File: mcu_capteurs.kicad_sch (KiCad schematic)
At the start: 71 parts, among them J15 BOOT0, J4 STLINK, SW1 435431019840, U2 TCA9517DR, U3 WSEN-PDUS, U4 STM32G474CEUx, Y1 16 MHz

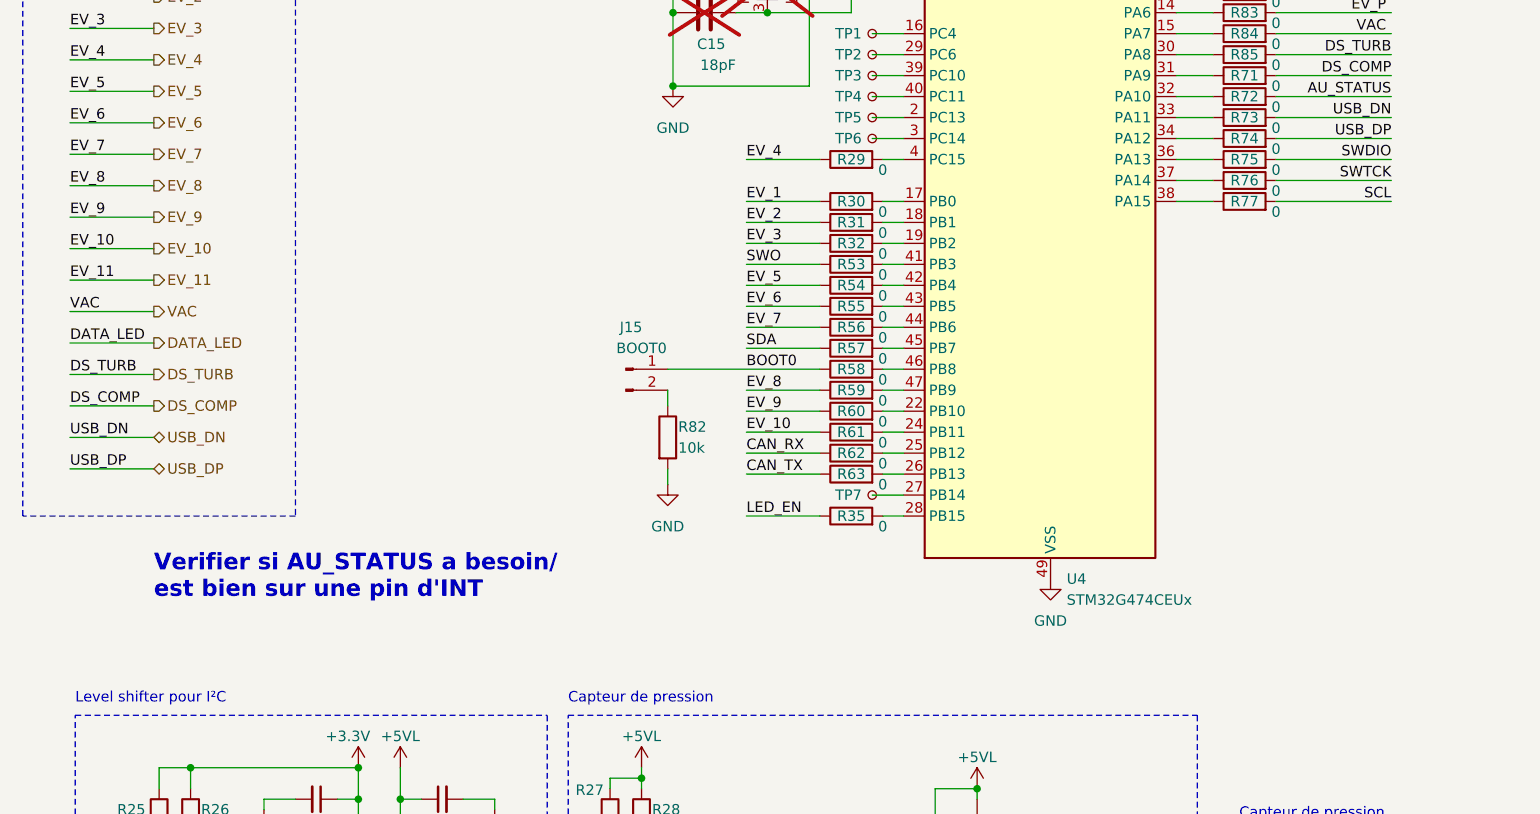
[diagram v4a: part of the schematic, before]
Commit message: placement en cours, remplacement diode schotcky, customisation empreinte capteur pression, suppression R pour les signaux figé du uC (SW, BOOT, etc). TODO avancer placement, ajouter LED
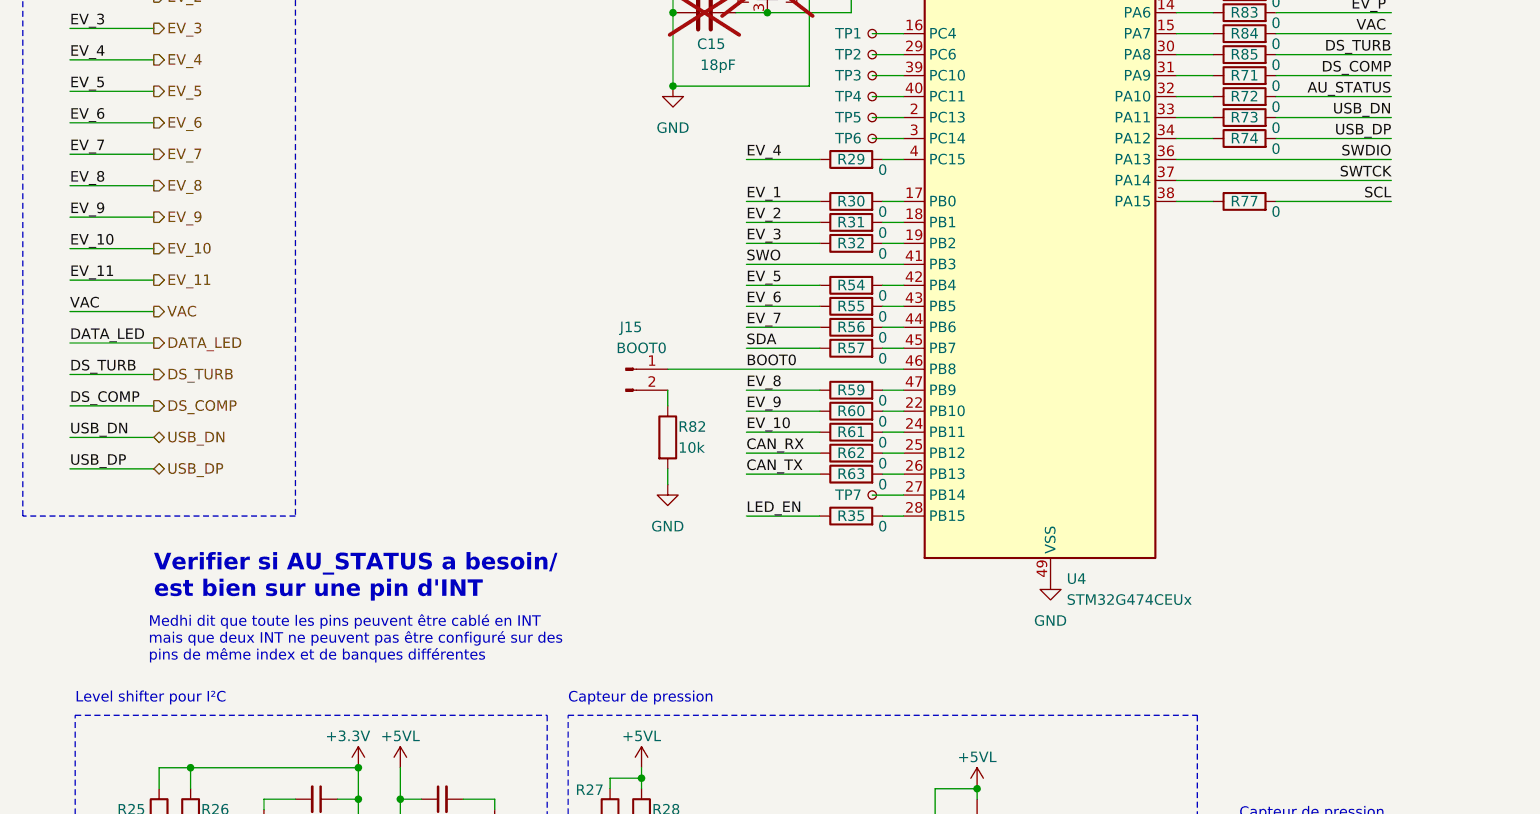
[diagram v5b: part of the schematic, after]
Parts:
- removed R53, R58, R75, R76: 0, Resistor_SMD:R_0402_1005Metric, symbol Device:R
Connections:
- net BOOT0: now also U4.46 (PB8)
- net SWDIO: now also U4.36 (PA13)
- net SWO: now also U4.41 (PB3)
- net SWTCK: now also U4.37 (PA14)
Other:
- note added: "Medhi dit que toute les pins peuvent être cablé en INT mais que deux INT ne peuvent pas être configuré sur des pins de même index et de banques différentes"

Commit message: placement composant (carte distributeur)
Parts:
- U4: footprint Package_DFN_QFN:QFN-48-1EP_7x7mm_P0.5mm_EP5.6x5.6mm -> 12V-actuators_pcb:QFN-48-1EP_7x7mm_P0.5mm_EP5.5x5.5mm
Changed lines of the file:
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@@
 			)
 		)
-		(property "Footprint" "Package_DFN_QFN:QFN-48-1EP_7x7mm_P0.5mm_EP5.6x5.6mm"
+		(property "Footprint" "12V-actuators_pcb:QFN-48-1EP_7x7mm_P0.5mm_EP5.5x5.5mm"
 			(at 127 129.54 0)
 			(effects

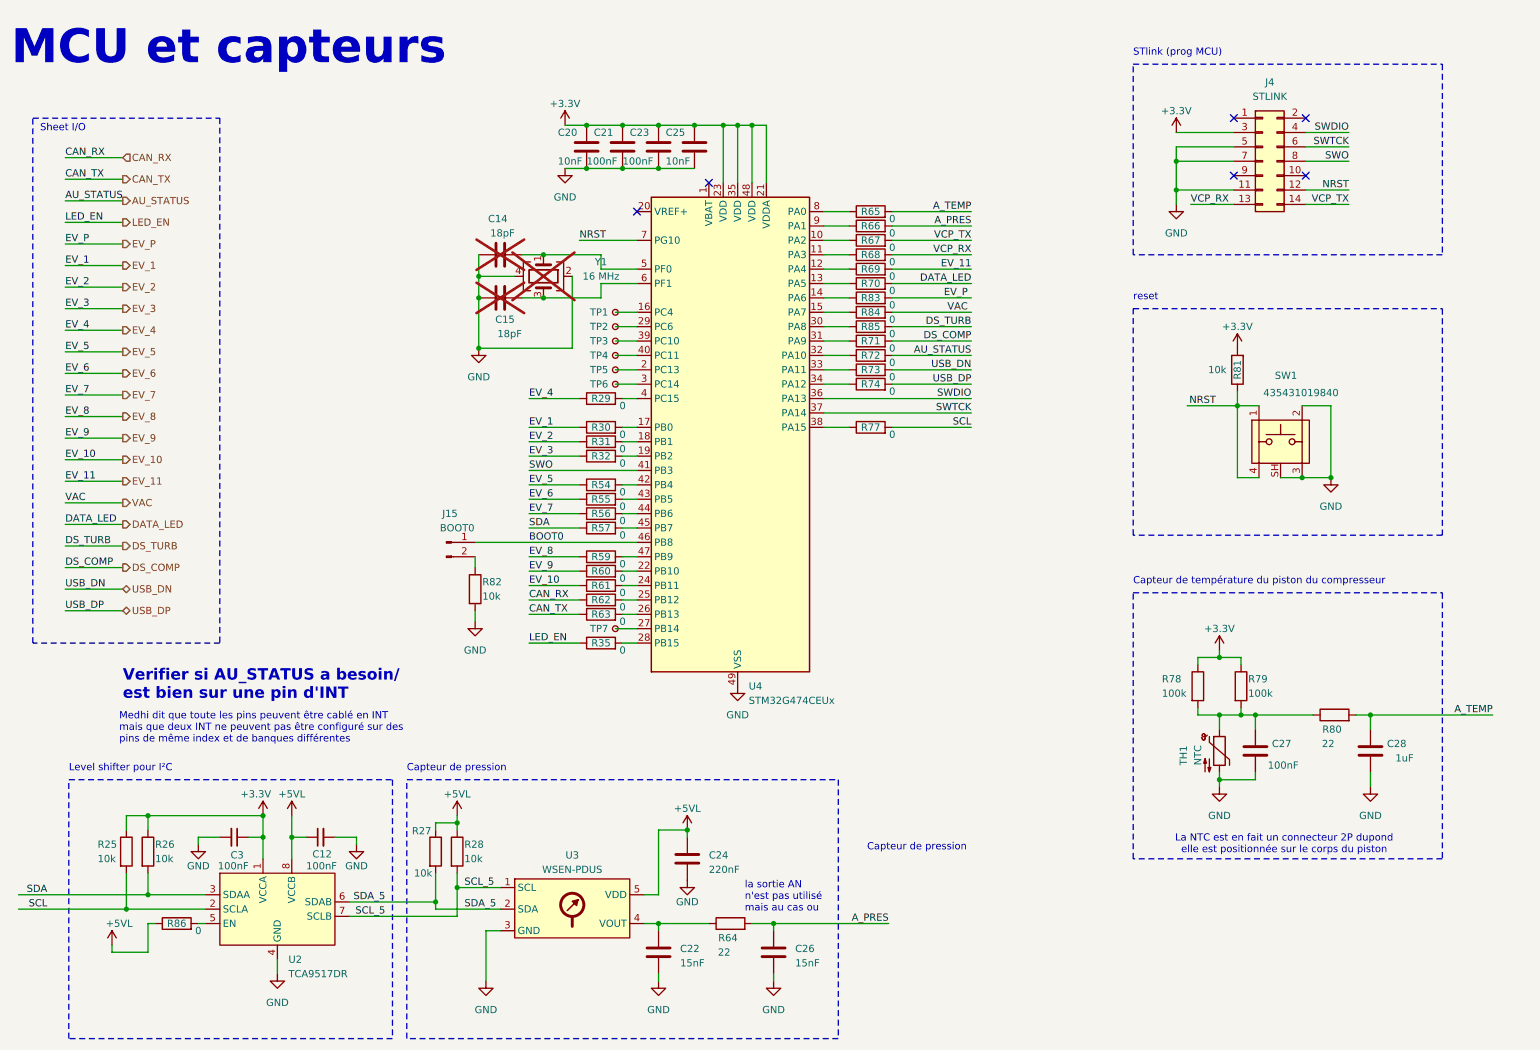
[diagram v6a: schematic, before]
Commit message: ajout regle routage JLCPCB, fin placement grossier et debut reassignation. ajout de led temoin, homogeinisation empreinte passif et remplacement 0ohm par empreintre jumper PCB 0402.
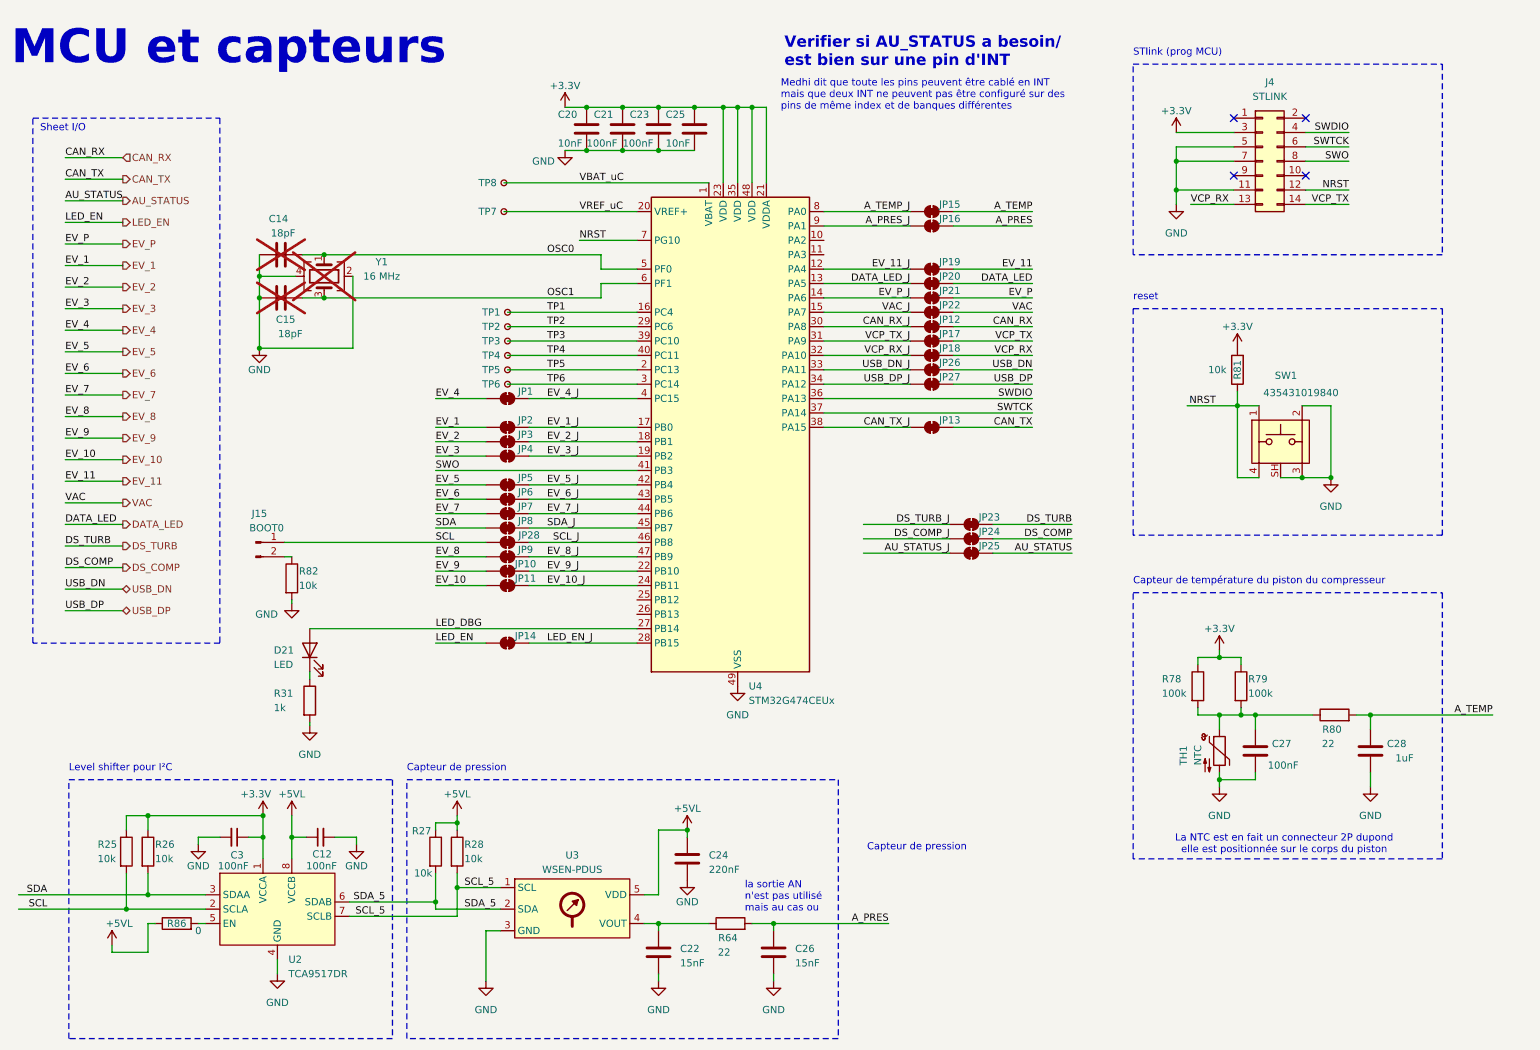
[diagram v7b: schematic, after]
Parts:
- removed R29, R30, R32, R35, R54, R55, R56, R57, R59, R60, R61, R62, R63, R65, R66, R67, R68, R69, R70, R71, R72, R73, R74, R77, R83, R84, R85: 0, Resistor_SMD:R_0402_1005Metric, symbol Device:R
- added D21: LED, LED_SMD:LED_0603_1608Metric, symbol Device:LED
- added JP1, JP10, JP11, JP12, JP13, JP14, JP15, JP16, JP17, JP18, JP19, JP2, JP20, JP21, JP22, JP23, JP24, JP25, JP26, JP27, JP28, JP3, JP4, JP5, JP6, JP7, JP8, JP9: SolderJumper_2_Bridged, 12V-actuators_pcb:R_0402_1005Metric_jumperClosed, symbol Jumper:SolderJumper_2_Bridged
- added TP8: TestPoint_Small, TestPoint:TestPoint_Pad_D1.0mm, symbol Connector:TestPoint_Small
- R31: value 0 -> 1k; footprint Resistor_SMD:R_0402_1005Metric -> Resistor_SMD:R_0603_1608Metric
- R81: footprint Resistor_SMD:R_0402_1005Metric -> Resistor_SMD:R_0603_1608Metric
- R86: footprint Resistor_SMD:R_0402_1005Metric -> 12V-actuators_pcb:R_0402_1005Metric_jumperClosed; now left out of the parts list
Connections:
- net AU_STATUS: now also JP25.2 (B)
- net A_PRES: now also JP16.2 (B)
- net A_TEMP: now also JP15.2 (B)
- net CAN_RX: now also JP12.1 (A)
- net CAN_TX: now also JP13.1 (A)
- net DATA_LED: now also JP20.2 (B)
- net DS_COMP: now also JP24.2 (B)
- net DS_TURB: now also JP23.2 (B)
- net EV_1: now also JP2.1 (A)
- net EV_10: now also JP11.1 (A)
- net EV_11: now also JP19.2 (B)
- net EV_2: now also JP3.1 (A); no longer R31.1
- net EV_3: now also JP4.1 (A)
- net EV_4: now also JP1.1 (A)
- net EV_5: now also JP5.1 (A)
- net EV_6: now also JP6.1 (A)
- net EV_7: now also JP7.1 (A)
- net EV_8: now also JP9.1 (A)
- net EV_9: now also JP10.1 (A)
- net EV_P: now also JP21.2 (B)
- net GND: now also R31.2
- net LED_EN: now also JP14.1 (A)
- net SCL: now also J15.1 (Pin_1), JP28.2 (B)
- net SDA: now also JP8.1 (A)
- net USB_DN: now also JP26.2 (B)
- net USB_DP: now also JP27.2 (B)
- net VAC: now also JP22.2 (B)
- net VCP_RX: now also JP18.2 (B)
- net VCP_TX: now also JP17.2 (B)
- net TP2: now reaches TP2.1, U4.29 (PC6)
- net TP5: now reaches TP5.1, U4.2 (PC13)
- net EV_3_J: now reaches U4.19 (PB2)
- net EV_3_J: now also JP4.2 (B)
- net EV_P_J: now reaches U4.14 (PA6)
- net EV_P_J: now also JP21.1 (A)
- net CAN_TX_J: now reaches U4.38 (PA15)
- net CAN_TX_J: now also JP13.2 (B)
- net VCP_RX_J: now reaches U4.32 (PA10)
- net VCP_RX_J: now also JP18.1 (A)
- net OSC0: now reaches C14.2, U4.5 (PF0), Y1.1
- net OSC1: now reaches C15.2, U4.6 (PF1), Y1.3
- net EV_4_J: now reaches U4.4 (PC15)
- net EV_4_J: now also JP1.2 (B)
- net A_PRES_J: now reaches U4.9 (PA1)
- net A_PRES_J: now also JP16.1 (A)
- net TP1: now reaches TP1.1, U4.16 (PC4)
- net EV_11_J: now reaches U4.12 (PA4)
- net EV_11_J: now also JP19.1 (A)
- net LED_EN_J: now reaches U4.28 (PB15)
- net LED_EN_J: now also JP14.2 (B)
- net TP3: now reaches TP3.1, U4.39 (PC10)
- net EV_7_J: now reaches U4.44 (PB6)
- net EV_7_J: now also JP7.2 (B)
- net DATA_LED_J: now reaches U4.13 (PA5)
- net DATA_LED_J: now also JP20.1 (A)
- net EV_5_J: now reaches U4.42 (PB4)
- net EV_5_J: now also JP5.2 (B)
- net CAN_RX_J: now reaches U4.30 (PA8)
- net CAN_RX_J: now also JP12.2 (B)
- net SDA_J: now reaches U4.45 (PB7)
- net SDA_J: now also JP8.2 (B)
- net EV_10_J: now reaches U4.24 (PB11)
- net EV_10_J: now also JP11.2 (B)
- net VBAT_uC: now reaches U4.1 (VBAT)
- net VBAT_uC: now also TP8.1
- net VAC_J: now reaches U4.15 (PA7)
- net VAC_J: now also JP22.1 (A)
- net EV_1_J: now reaches U4.17 (PB0)
- net EV_1_J: now also JP2.2 (B)
- net EV_2_J: now reaches U4.18 (PB1)
- net EV_2_J: now also JP3.2 (B); no longer R31.2
- net VREF_uC: now reaches U4.20 (VREF+)
- net VREF_uC: now also TP7.1
- net EV_9_J: now reaches U4.22 (PB10)
- net EV_9_J: now also JP10.2 (B)
- net LED_DBG: now reaches U4.27 (PB14)
- net LED_DBG: now also D21.2 (A); no longer TP7.1
- net TP6: now reaches TP6.1, U4.3 (PC14)
- net VCP_TX_J: now reaches U4.31 (PA9)
- net VCP_TX_J: now also JP17.1 (A)
- net USB_DN_J: now reaches U4.33 (PA11)
- net USB_DN_J: now also JP26.1 (A)
- net USB_DP_J: now reaches U4.34 (PA12)
- net USB_DP_J: now also JP27.1 (A)
- net TP4: now reaches TP4.1, U4.40 (PC11)
- net EV_6_J: now reaches U4.43 (PB5)
- net EV_6_J: now also JP6.2 (B)
- net EV_8_J: now reaches U4.47 (PB9)
- net EV_8_J: now also JP9.2 (B)
- net A_TEMP_J: now reaches U4.8 (PA0)
- net A_TEMP_J: now also JP15.1 (A)
- net BOOT0 renamed SCL_J
- net SCL_J: now also JP28.1 (A); no longer J15.1 (Pin_1)
- new net: D21.1 (K), R31.1
- new net AU_STATUS_J: JP25.1 (A)
- new net DS_COMP_J: JP24.1 (A)
- new net DS_TURB_J: JP23.1 (A)
- no-connect marks 6 -> 4
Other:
- moved on the sheet: C14, C15, C20, C21, C23, C25, J15, R82, TP1, TP2, TP3, TP4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
